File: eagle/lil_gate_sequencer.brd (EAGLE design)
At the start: 100 x 80 mm, 63 parts, among them IC1 4093N, IC2 4017N, Q1 2N3904, Q2 2N3904

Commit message: jameco toggle part
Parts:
- removed LONG_STEP, S10, S11, S2, S3, S4, S5, S6, S7, S8, S9: (no value), adafruit:EG1218
- added LENGTH, STEP_1, STEP_2, STEP_3, STEP_4, STEP_5, STEP_6, STEP_7, STEP_8, STEP_9, U$10: MTS-102-C4, jameco:MTS-102-C4
- LOOP, ON_OFF: value (none) -> MTS-102-C4; device adafruit:EG1218 -> jameco:MTS-102-C4
- moved ON_OFF 151.8 mm to (-200.7, 12.7)
- moved FB1 110.5 mm to (29.2, 59.7), turned to 90 degrees
- moved PWR1 67.8 mm to (19.1, 48.3), turned to 90 degrees
- moved LOOP 44.5 mm to (-94.0, 12.7)
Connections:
- net +12V: now also LENGTH.P$1; no longer LONG_STEP.S
- net N$12: now also LENGTH.P$3; no longer LONG_STEP.O
- net N$13: now also STEP_1.P$2; no longer S2.P
- net N$14: now also LOOP.P$3; no longer LOOP.O
- net N$16: now also STEP_2.P$2; no longer S3.P
- net N$18: now also STEP_3.P$2; no longer S4.P
- net N$20: now also STEP_4.P$2; no longer S5.P
- net N$22: now also STEP_5.P$2; no longer S6.P
- net N$24: now also STEP_6.P$2; no longer S7.P
- net N$26: now also STEP_7.P$2; no longer S8.P
- net N$28: now also STEP_8.P$2; no longer S9.P
- net N$30: now also STEP_9.P$2; no longer S10.P
- net N$32: now also U$10.P$2; no longer S11.P
- net N$34: now also LOOP.P$2, STEP_2.P$3, STEP_3.P$3, STEP_4.P$3, STEP_5.P$3, STEP_6.P$3, STEP_7.P$3, STEP_8.P$3, STEP_9.P$3, U$10.P$3; no longer LOOP.P, S10.O, S11.O, S3.O, S4.O, S5.O, S6.O, S7.O, S8.O, S9.O
- net N$36: now also ON_OFF.P$1, STEP_1.P$1, STEP_2.P$1, STEP_3.P$1, STEP_4.P$1, STEP_5.P$1, STEP_6.P$1, STEP_7.P$1, STEP_8.P$1, STEP_9.P$1, U$10.P$1; no longer ON_OFF.S, S10.S, S11.S, S2.S, S3.S, S4.S, S5.S, S6.S, S7.S, S8.S, S9.S
- net N$37: now also LENGTH.P$2; no longer LONG_STEP.P
- net N$38: now also ON_OFF.P$2; no longer ON_OFF.P
- net N$6: now also IC1.11
- net N$9: now also LOOP.P$1; no longer LOOP.S

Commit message: layout begins
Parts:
- removed LENGTH, ON_OFF, U$10: MTS-102-C4, jameco:MTS-102-C4
- added ENABLE_1, ENABLE_2, LENGTH_1, LENGTH_LONG, LENGTH_SHORT, LOOP_1, LOOP_ON: LSP11, solpad:LSP11
- added STEP_10: MTS-102-C4, jameco:MTS-102-C4
- D1: value 1N4148DO35-7 -> 1N4148DO35-10; device diode:DO35-7 -> diode:DO35-10
- LOOP: value MTS-102-C4 -> LSP11; device jameco:MTS-102-C4 -> solpad:LSP11
- R10: device rcl:0207/7 -> rcl:0309/12
- moved STEP_9 194.6 mm to (20.3, 1.91)
- moved STEP_8 194.0 mm to (28.6, 1.91)
- moved STEP_7 193.3 mm to (36.8, 1.91)
- moved STEP_6 192.7 mm to (45.1, 1.91)
- moved STEP_5 192.1 mm to (53.3, 1.91)
- moved STEP_4 191.4 mm to (61.6, 1.91)
- moved STEP_3 190.8 mm to (69.8, 1.91)
- moved STEP_2 190.2 mm to (78.1, 1.91)
- moved STEP_1 189.5 mm to (86.4, 1.91)
- moved D2 176.4 mm to (90.2, 23.5), turned to 90 degrees
- moved R7 168.6 mm to (82.5, 53.3), turned to 270 degrees
- moved R6 166.1 mm to (90.2, 53.3), turned to 270 degrees
- moved LED3 152.4 mm to (73.7, 32.4), turned to 90 degrees
- moved LED2 148.0 mm to (81.9, 32.4), turned to 90 degrees
- moved R8 145.1 mm to (77.5, 43.2), turned to 180 degrees
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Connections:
- net +12V: now also LENGTH_LONG.MP; no longer LENGTH.P$1
- net GND: now also CLK.P$2
- net N$12: now also LENGTH_SHORT.MP; no longer LENGTH.P$3
- net N$14: now also LOOP_1.MP; no longer LOOP.P$3
- net N$32: now also STEP_10.P$2; no longer U$10.P$2
- net N$34: now also LOOP.MP, STEP_10.P$3; no longer LOOP.P$2, U$10.P$3
- net N$36: now also ENABLE_1.MP, STEP_10.P$1; no longer ON_OFF.P$1, U$10.P$1
- net N$37: now also LENGTH_1.MP; no longer LENGTH.P$2
- net N$38: now also ENABLE_2.MP; no longer ON_OFF.P$2
- net N$9: now also LOOP_ON.MP; no longer LOOP.P$1

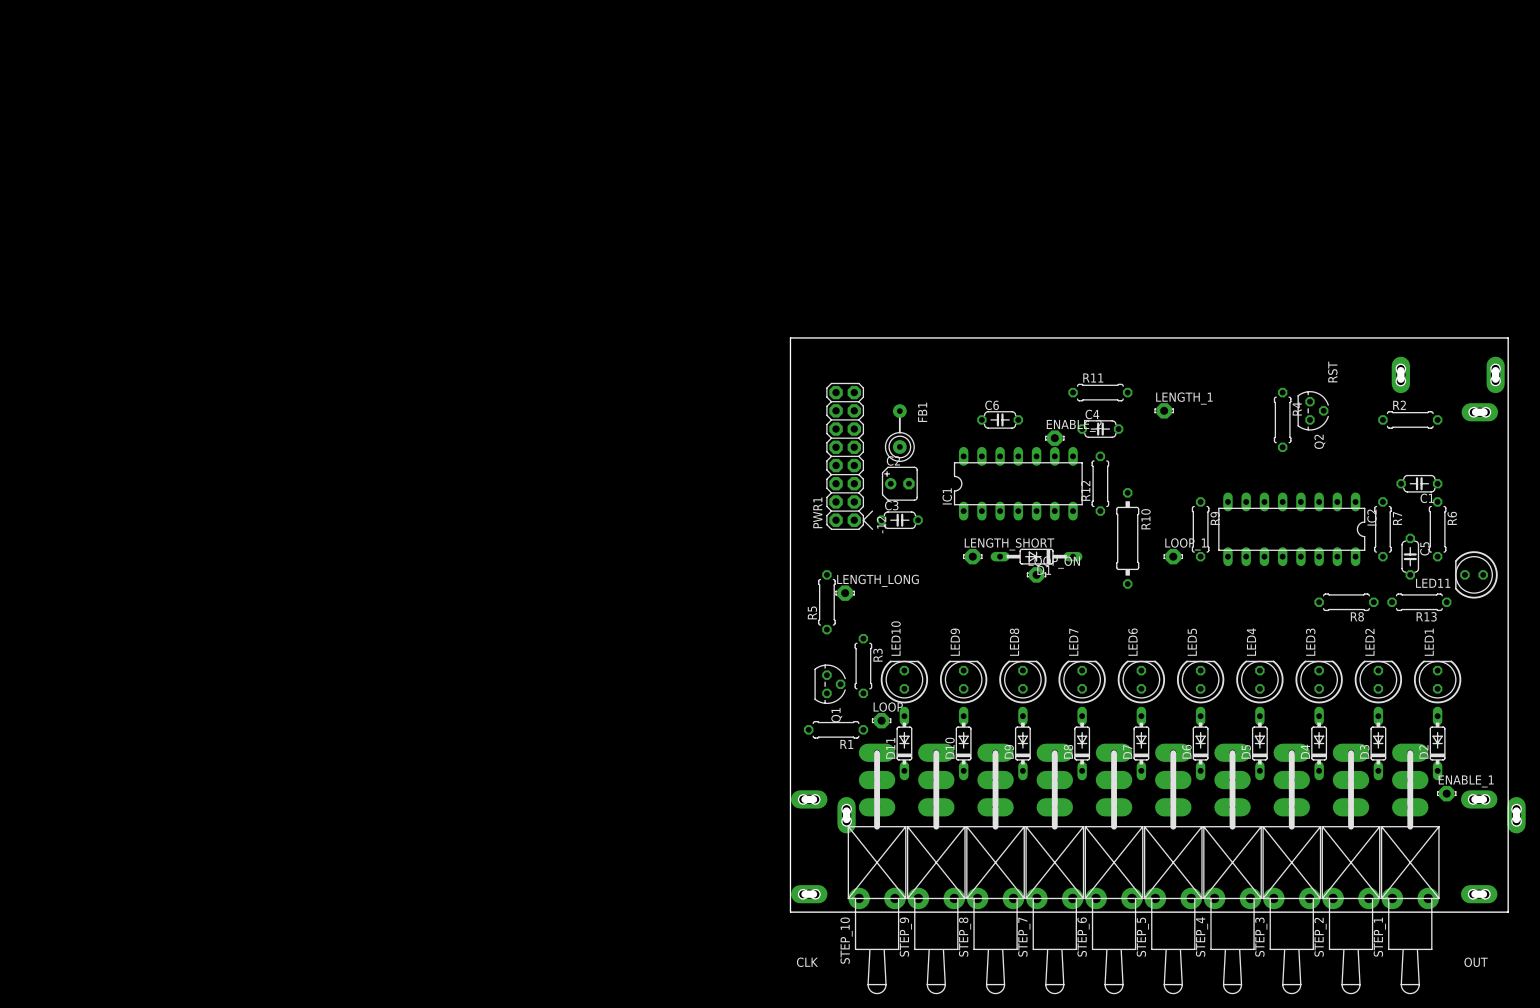
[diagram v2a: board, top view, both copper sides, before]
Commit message: routed the 4017
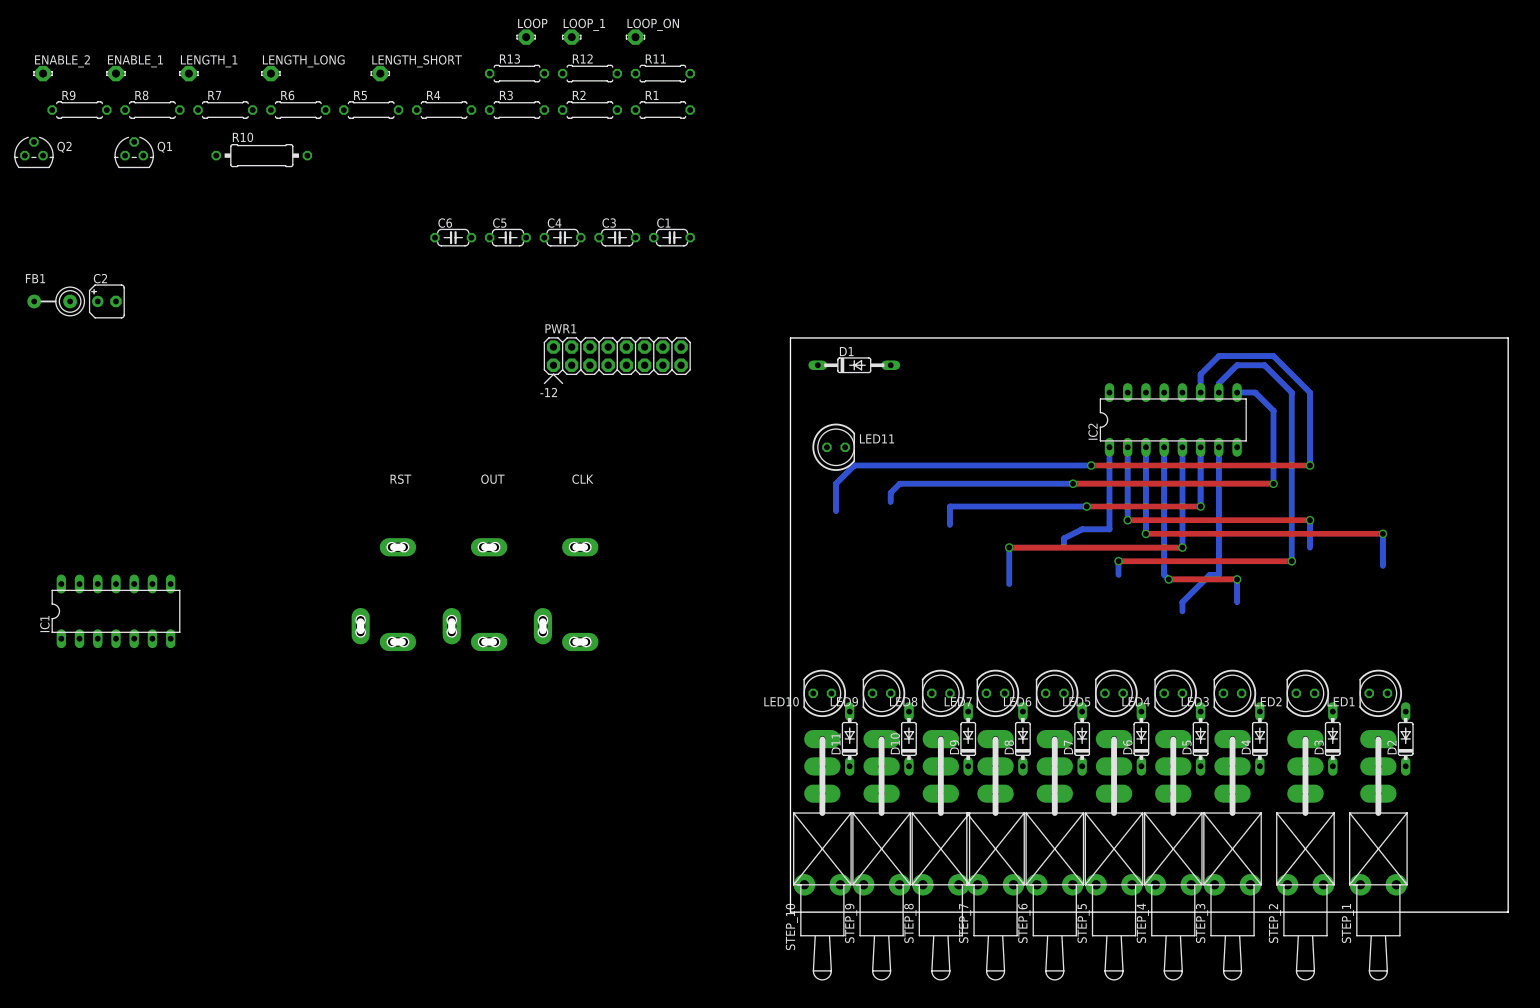
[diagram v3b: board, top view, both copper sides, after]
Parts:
- moved ENABLE_1 210.8 mm to (-94.0, 116.8)
- moved Q2 181.3 mm to (-105.4, 105.4), turned to 0 degrees
- moved R8 180.0 mm to (-88.9, 111.8), turned to 0 degrees
- moved R7 171.5 mm to (-78.7, 111.8), turned to 0 degrees
- moved R6 169.2 mm to (-68.6, 111.8), turned to 0 degrees
- moved R9 166.8 mm to (-99.1, 111.8), turned to 0 degrees
- moved OUT 157.3 mm to (-47.0, 53.3), turned to 0 degrees
- moved ENABLE_2 149.8 mm to (-104.1, 116.8)
- moved R13 145.7 mm to (-38.1, 116.8), turned to 0 degrees
- moved LENGTH_1 143.8 mm to (-83.8, 116.8)
- moved RST 143.2 mm to (-59.7, 53.3), turned to 0 degrees
- moved C5 133.4 mm to (-39.4, 94.0), turned to 0 degrees
- moved R10 131.9 mm to (-73.7, 105.4), turned to 0 degrees
- moved IC1 127.0 mm to (-94.0, 41.9)
- moved R4 124.6 mm to (-48.3, 111.8), turned to 0 degrees
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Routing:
- net N$33: track 0.00 -> 102.0 mm, vias 0 -> 2
- net N$31: track 0.00 -> 71.4 mm, vias 0 -> 2
- net N$23: track 0.00 -> 63.6 mm, vias 0 -> 2
- net N$15: track 0.00 -> 49.5 mm, vias 0 -> 2
- net N$29: track 0.00 -> 45.7 mm, vias 0 -> 2
- net N$27: track 0.00 -> 43.2 mm, vias 0 -> 2
- net N$17: track 0.00 -> 39.4 mm, vias 0 -> 2
- net N$19: track 0.00 -> 31.4 mm, vias 0 -> 2
- net N$21: track 0.00 -> 25.7 mm
- net N$25: track 0.00 -> 19.3 mm

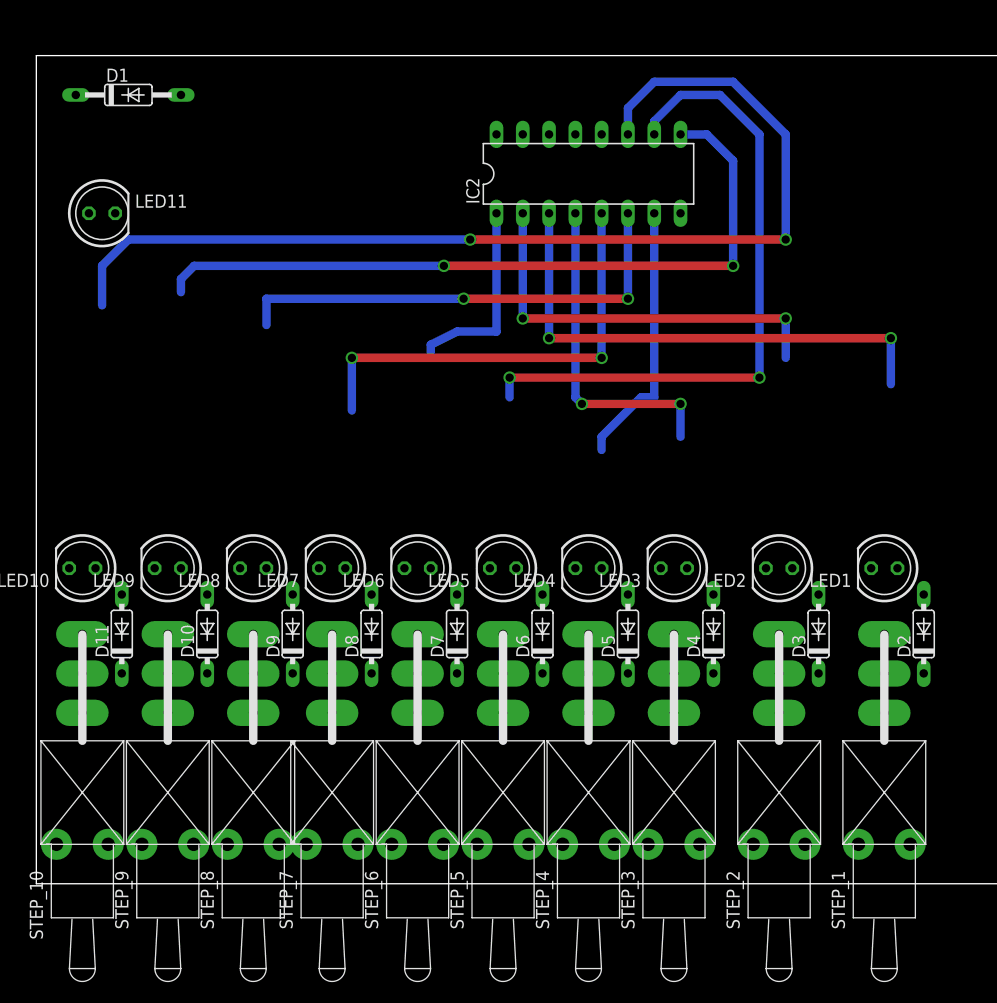
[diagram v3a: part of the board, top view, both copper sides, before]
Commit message: switch and diode routes
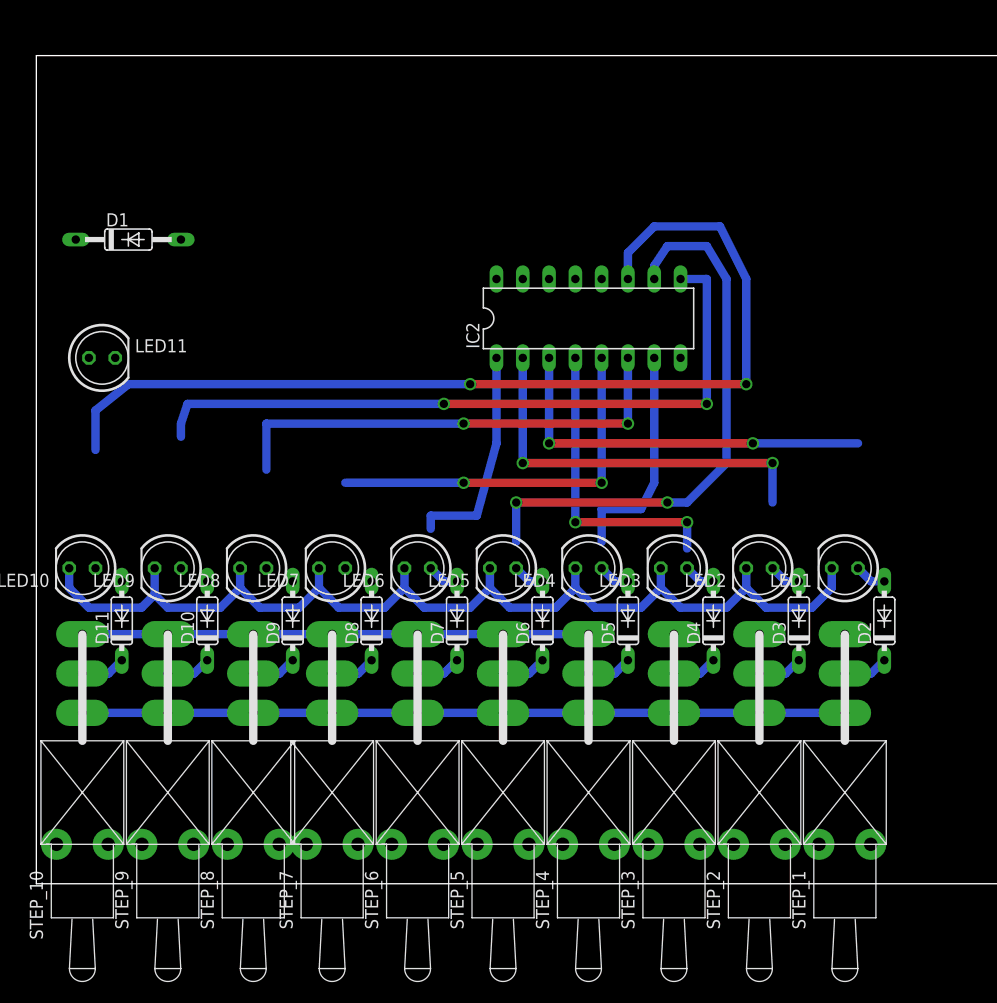
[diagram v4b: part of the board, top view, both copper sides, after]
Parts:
- moved D1 14.0 mm to (8.89, 62.2)
- moved IC2 14.0 mm to (53.3, 54.6)
- moved LED11 14.0 mm to (6.35, 50.8)
- moved D2 4.02 mm to (81.9, 25.4)
- moved LED1 3.81 mm to (78.1, 30.5)
- moved STEP_1 3.81 mm to (78.1, 3.81)
- moved D3 2.29 mm to (73.7, 25.4)
- moved LED2 1.91 mm to (69.8, 30.5)
- moved STEP_2 1.91 mm to (69.8, 3.81)
- moved D10 1.27 mm to (16.5, 25.4)
- moved D11 1.27 mm to (8.26, 25.4)
- moved D4 1.27 mm to (65.4, 25.4)
- moved D5 1.27 mm to (57.1, 25.4)
- moved D6 1.27 mm to (48.9, 25.4)
- moved D7 1.27 mm to (40.6, 25.4)
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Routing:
- net N$35: track 0.00 -> 107.0 mm
- net N$36: track 0.00 -> 73.7 mm
- net N$34: track 0.00 -> 48.9 mm
- net N$15: track 49.5 -> 41.2 mm
- net N$27: track 43.2 -> 36.8 mm
- net N$33: track 102.0 -> 95.9 mm
- net N$23: track 63.6 -> 57.6 mm
- net N$25: track 19.3 -> 24.3 mm
- net N$30: track 0.00 -> 4.34 mm
- net N$28: track 0.00 -> 4.34 mm
- net N$24: track 0.00 -> 4.34 mm
- net N$22: track 0.00 -> 4.34 mm
- net N$18: track 0.00 -> 4.34 mm
- net N$16: track 0.00 -> 4.34 mm
- net N$13: track 0.00 -> 4.34 mm
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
